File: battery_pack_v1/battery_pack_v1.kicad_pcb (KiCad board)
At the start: 4 copper layers, 88 x 94.5 mm, 28 parts, among them J1 Battery Input, J2 Negative 1, J3 Pos 1, J4 Pos 2, J5 Negative 2, Q1 IRF7458, Q2 IRF7458, U1 R5460N208AA

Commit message: branch_upload_test
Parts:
- removed J2: Negative 1, Battery Holders:BAT-SMD_MY-18650-02
- removed J3: Pos 1, Battery Holders:BAT-SMD_MY-18650-02
- removed J4: Pos 2, Battery Holders:BAT-SMD_MY-18650-02
- removed J5: Negative 2, Battery Holders:BAT-SMD_MY-18650-02
- added BT3: Battery_Cell, Battery Holders:BAT-TH_BH-18650-A6AJ012, F.Cu at (188.0, 89.4)
- added BT4: Battery_Cell, Battery Holders:BAT-TH_BH-18650-A6AJ012, F.Cu at (124.0, 89.4)
- J1: footprint DF11:CONN-SMD_12P-P2.00_DF11CZ-12DP -> Connector_Hirose:Hirose_DF11-12DP-2DSA_2x06_P2.00mm_Vertical
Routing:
- net BM: track 162.9 -> 136.0 mm
- net PACK+: track 104.3 -> 98.0 mm
- net B-: track 91.4 -> 85.5 mm

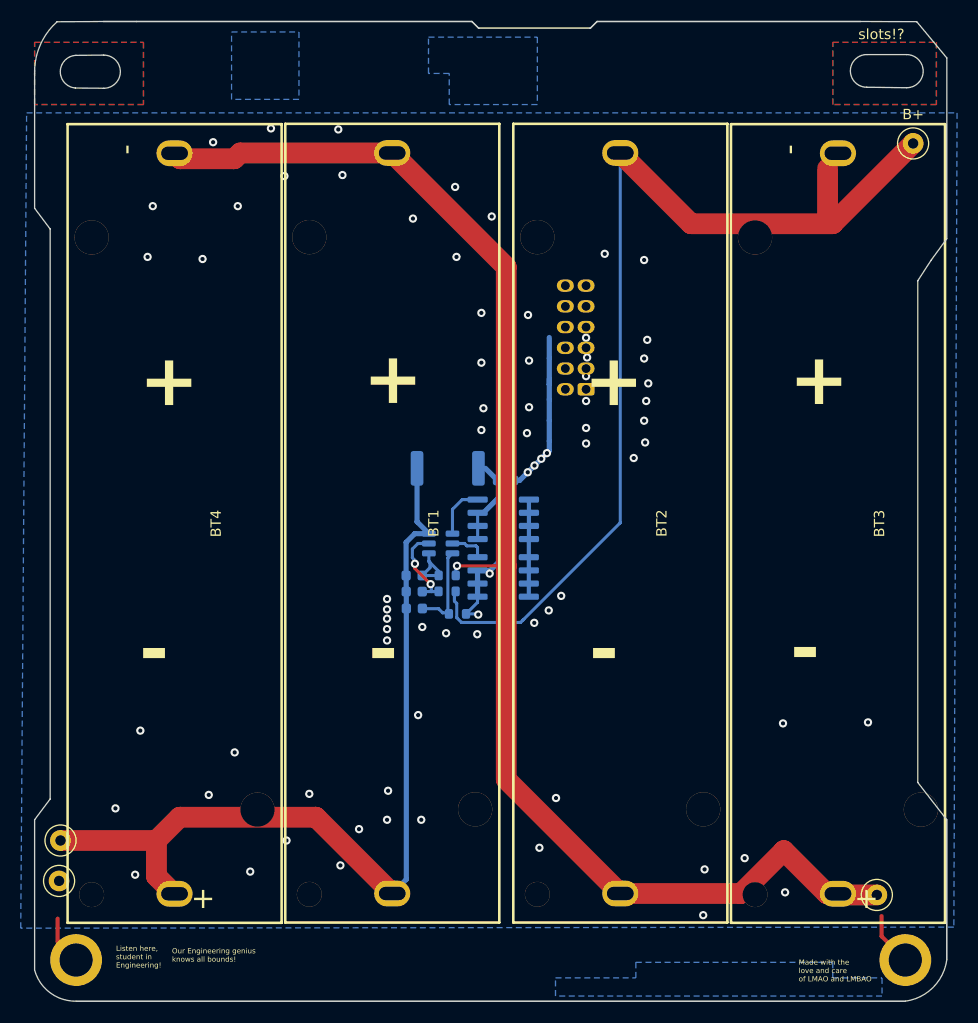
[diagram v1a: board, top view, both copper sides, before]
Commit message: Modified traces to be out of way of mounting holes
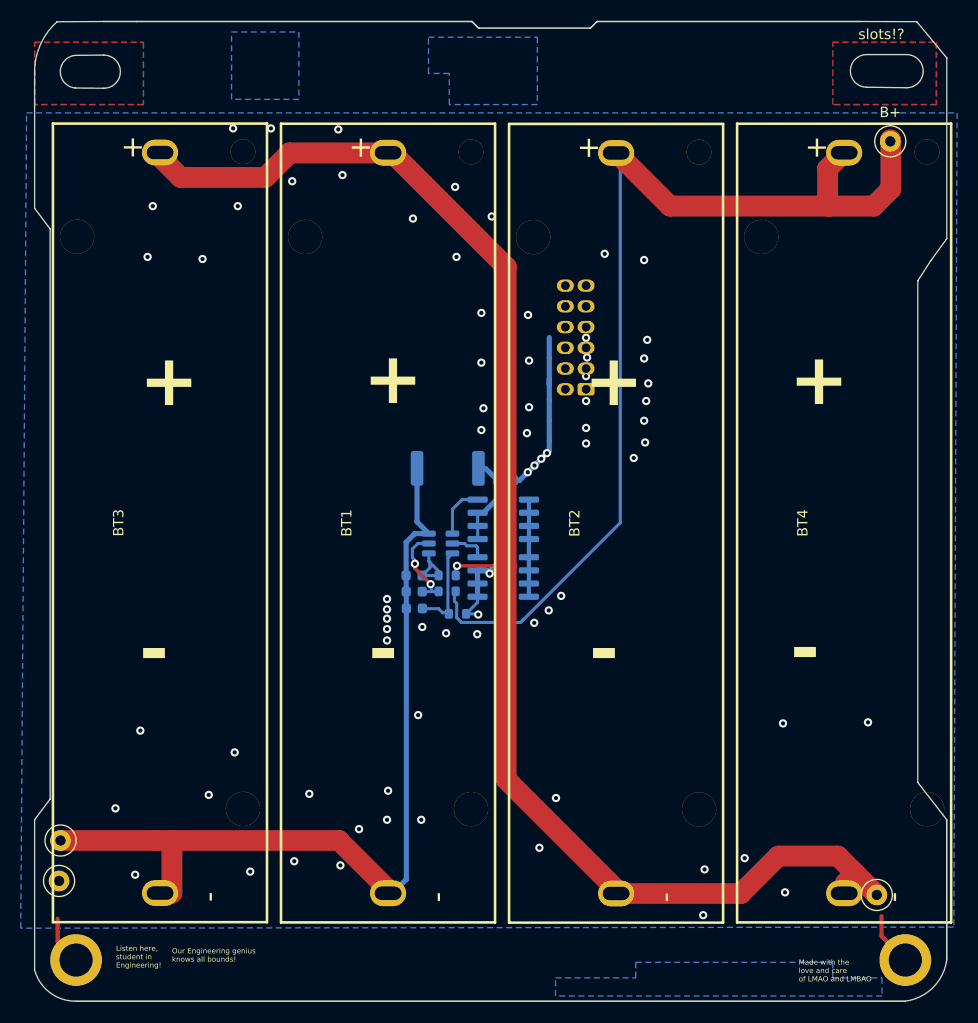
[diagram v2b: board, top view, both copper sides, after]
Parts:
- BT1, BT2, BT3, BT4: footprint Battery Holders:BAT-TH_BH-18650-A6AJ012 -> Battery Holders:BAT-TH_BH-18650-A6AJ012_MODIFICATION
- moved BT3 65.4 mm to (122.6, 89.3), turned to 90 degrees
- moved BT4 64.6 mm to (188.6, 89.4), turned to 90 degrees
- moved TP5 2.21 mm to (193.1, 52.5)
- moved BT1 0.40 mm to (144.6, 89.4), turned to 90 degrees
- moved BT2 0.40 mm to (166.6, 89.4), turned to 90 degrees
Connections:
- BT3 pad 1: PACK+ -> BM
- BT3 pad 2: BM -> B-
- BT4 pad 1: BM -> PACK+
- BT4 pad 2: B- -> BM
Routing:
- net BM: track 136.0 -> 139.9 mm
- net B-: track 85.5 -> 82.6 mm
- added copper zone on B.Cu, net PACK+
- removed copper zone on B.Cu, net PACK-
